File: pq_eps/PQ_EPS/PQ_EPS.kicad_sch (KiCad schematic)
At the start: 87 parts, among them IC1 DS2782E+, IC2 ISL9120IRTNZ, J1 CES-110-02-L-S, J2 CES-110-02-L-S, J3 CES-110-02-L-S, J4 CES-110-02-L-S, Q1 SIR424DP, U1 SPV1040TTR, U2 SPV1040TTR, U3 SPV1040TTR, U4 LTC4040EUFD#PBF

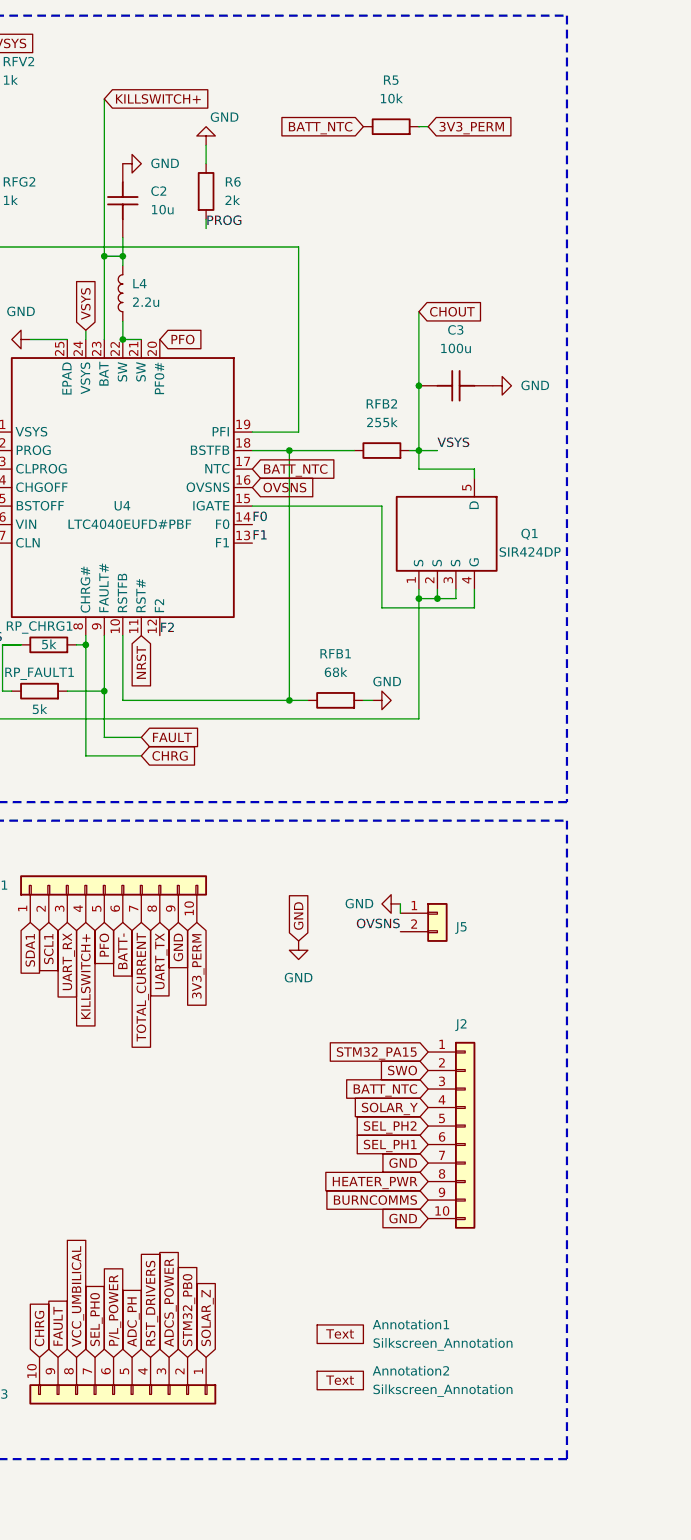
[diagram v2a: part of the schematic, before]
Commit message: small changes: change ID R5 to Rbias, add snail logo, and swap SOLARZ with GND
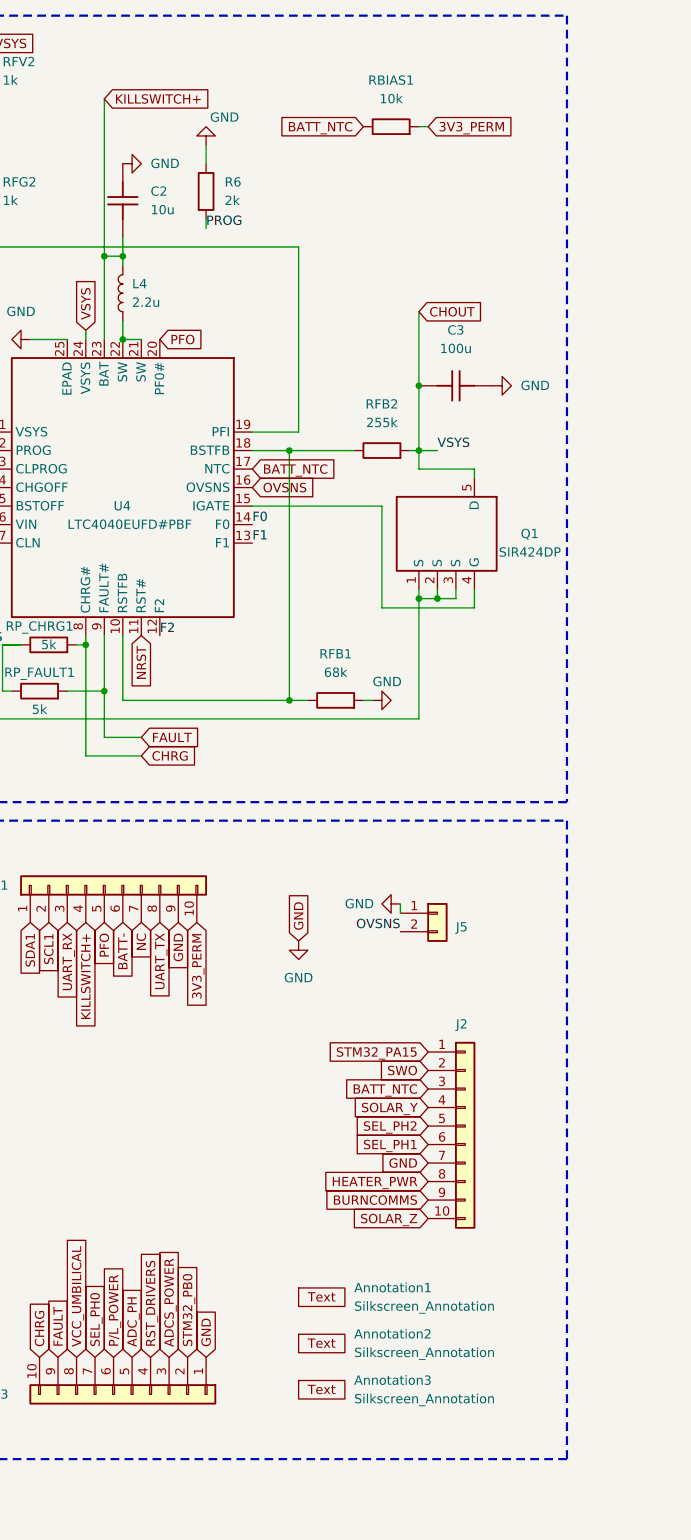
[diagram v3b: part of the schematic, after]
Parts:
- added Annotation3: Silkscreen_Annotation, symbols-nsl:Snail, symbol symbols-nsl:Silkscreen_Annotation
- renumbered R5 to RBIAS1
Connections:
- net GND: now also J3.1 (Pin_1); no longer J2.10 (Pin_10)
- net SOLAR_Z: now also J2.10 (Pin_10); no longer J3.1 (Pin_1)
- net TOTAL_CURRENT renamed NC
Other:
- moved on the sheet: Annotation1, Annotation2
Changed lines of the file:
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@@
     )
   )
-  (global_label "SOLAR_Z" (shape input) (at 297.18 210.82 90) (fields_autoplaced)
+  (global_label "GND" (shape input) (at 297.18 210.82 90) (fields_autoplaced)
     (effects (font (size 1.27 1.27)) (justify left))
-    (property "Intersheetrefs" "${INTERSHEET_REFS}" (at 297.1006 200.3031 90)
+    (property "Intersheetrefs" "${INTERSHEET_REFS}" (at 297.18 203.9643 90)
       (effects (font (size 1.27 1.27)) (justify left) hide)
     )
@@
     )
   )
-  (global_label "GND" (shape input) (at 327.66 191.77 180) (fields_autoplaced)
+  (global_label "SOLAR_Z" (shape input) (at 327.66 191.77 180) (fields_autoplaced)
     (effects (font (size 1.27 1.27)) (justify right))
-    (property "Intersheetrefs" "${INTERSHEET_REFS}" (at 321.3764 191.6906 0)
+    (property "Intersheetrefs" "${INTERSHEET_REFS}" (at 316.571 191.77 0)
       (effects (font (size 1.27 1.27)) (justify right) hide)
     )
@@
     )
   )
-  (global_label "TOTAL_CURRENT" (shape input) (at 288.29 151.13 270) (fields_autoplaced)
+  (global_label "NC" (shape input) (at 288.29 151.13 270) (fields_autoplaced)
     (effects (font (size 1.27 1.27)) (justify right))
-    (property "Intersheetrefs" "${INTERSHEET_REFS}" (at 288.2106 168.4807 90)
+    (property "Intersheetrefs" "${INTERSHEET_REFS}" (at 288.29 156.7157 90)
       (effects (font (size 1.27 1.27)) (justify right) hide)
     )
@@
     )
   )
-  (symbol (lib_id "symbols-nsl:Silkscreen_Annotation") (at 313.69 213.36 0) (unit 1)
+  (symbol (lib_id "symbols-nsl:Silkscreen_Annotation") (at 311.15 208.28 0) (unit 1)
     (in_bom yes) (on_board yes) (dnp no) (fields_autoplaced)
-    (property "Reference" "Annotation1" (at 320.04 206.375 0)
+    (property "Reference" "Annotation1" (at 317.5 201.295 0)
       (effects (font (size 1.27 1.27)) (justify left))
     )
-    (property "Value" "Silkscreen_Annotation" (at 320.04 208.915 0)
+    (property "Value" "Silkscreen_Annotation" (at 317.5 203.835 0)
       (effects (font (size 1.27 1.27)) (justify left))
     )
-    (property "Footprint" "symbols-nsl:Bridgemaker" (at 313.69 213.36 0)
+    (property "Footprint" "symbols-nsl:Bridgemaker" (at 311.15 208.28 0)
       (effects (font (size 1.27 1.27)) hide)
     )
-    (property "Datasheet" "" (at 313.69 213.36 0)
+    (property "Datasheet" "" (at 311.15 208.28 0)
       (effects (font (size 1.27 1.27)) hide)
     )
@@
   (symbol (lib_id "Device:R") (at 322.58 41.91 90) (unit 1)
     (in_bom yes) (on_board yes) (dnp no) (fields_autoplaced)
-    (property "Reference" "R5" (at 322.58 35.56 90)
+    (property "Reference" "RBIAS1" (at 322.58 35.56 90)
       (effects (font (size 1.27 1.27)))
     )
@@
       (project "PQ_EPS"
         (path "/369ed984-4bc0-4563-9a96-3c71b74c6c81"
-          (reference "R5") (unit 1)
+          (reference "RBIAS1") (unit 1)
         )
       )
@@
     )
   )
+  (symbol (lib_id "symbols-nsl:Silkscreen_Annotation") (at 311.15 220.98 0) (unit 1)
+    (in_bom yes) (on_board yes) (dnp no) (fields_autoplaced)
+    (property "Reference" "Annotation3" (at 317.5 213.995 0)
+      (effects (font (size 1.27 1.27)) (justify left))
+    )
+    (property "Value" "Silkscreen_Annotation" (at 317.5 216.535 0)
+      (effects (font (size 1.27 1.27)) (justify left))
+    )
+    (property "Footprint" "symbols-nsl:Snail" (at 311.15 220.98 0)
+      (effects (font (size 1.27 1.27)) hide)
+    )
+    (property "Datasheet" "" (at 311.15 220.98 0)
+      (effects (font (size 1.27 1.27)) hide)
+    )
+    (instances
+      (project "PQ_EPS"
+        (path "/369ed984-4bc0-4563-9a96-3c71b74c6c81"
+          (reference "Annotation3") (unit 1)
+        )
+      )
+    )
+  )
   (symbol (lib_id "Mechanical:MountingHole_Pad") (at 113.03 233.68 0) (unit 1)
     (in_bom yes) (on_board yes) (dnp no) (fields_autoplaced)
@@
     )
   )
-  (symbol (lib_id "symbols-nsl:Silkscreen_Annotation") (at 313.69 219.71 0) (unit 1)
+  (symbol (lib_id "symbols-nsl:Silkscreen_Annotation") (at 311.15 214.63 0) (unit 1)
     (in_bom yes) (on_board yes) (dnp no) (fields_autoplaced)
-    (property "Reference" "Annotation2" (at 320.04 212.725 0)
+    (property "Reference" "Annotation2" (at 317.5 207.645 0)
       (effects (font (size 1.27 1.27)) (justify left))
     )
-    (property "Value" "Silkscreen_Annotation" (at 320.04 215.265 0)
+    (property "Value" "Silkscreen_Annotation" (at 317.5 210.185 0)
       (effects (font (size 1.27 1.27)) (justify left))
     )
-    (property "Footprint" "symbols-nsl:NakNak" (at 313.69 219.71 0)
+    (property "Footprint" "symbols-nsl:NakNak" (at 311.15 214.63 0)
       (effects (font (size 1.27 1.27)) hide)
     )
-    (property "Datasheet" "" (at 313.69 219.71 0)
+    (property "Datasheet" "" (at 311.15 214.63 0)
       (effects (font (size 1.27 1.27)) hide)
     )

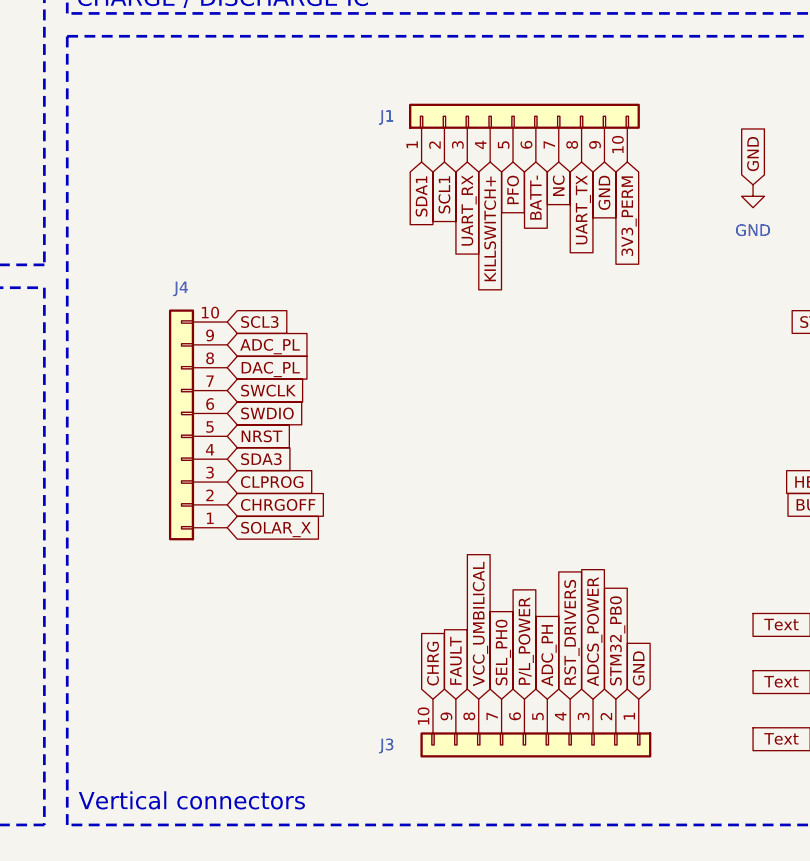
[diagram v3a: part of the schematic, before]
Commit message: change RST_DRIVERS to STM32_PA9, swap SCL3 with NC, and change NC to PH_PL
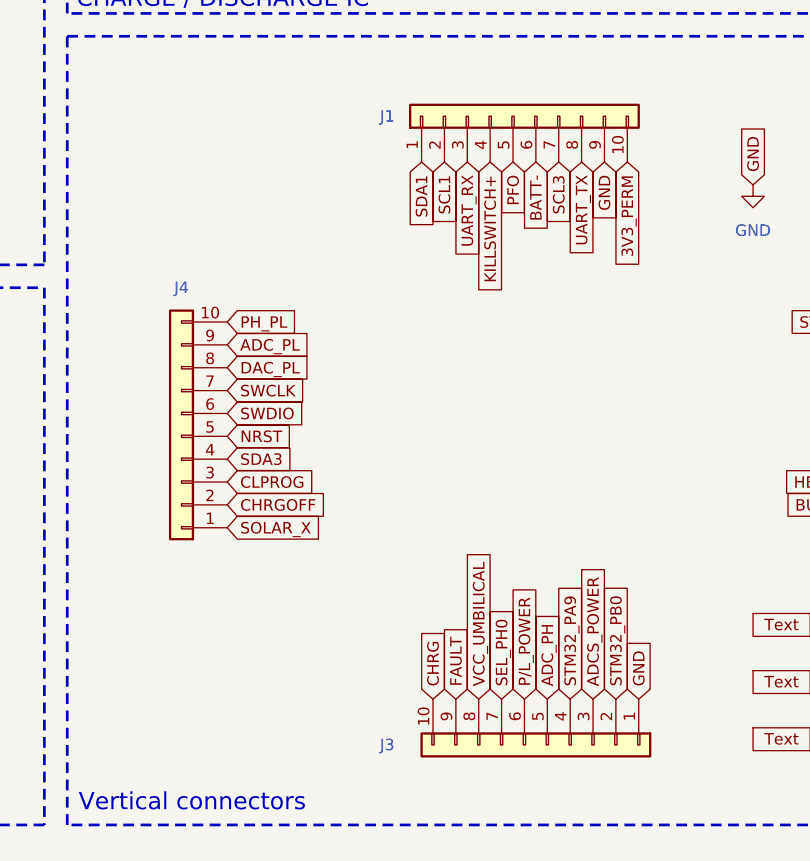
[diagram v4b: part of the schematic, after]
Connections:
- net NC is gone; now on net SCL3: J1.7 (Pin_7)
- net SCL3: no longer J4.10 (Pin_10)
- net RST_DRIVERS renamed STM32_PA9
- new net PH_PL: J4.10 (Pin_10)
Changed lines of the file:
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@@
     )
   )
-  (global_label "SCL3" (shape input) (at 251.46 168.91 0) (fields_autoplaced)
-    (effects (font (size 1.27 1.27)) (justify left))
-    (property "Intersheetrefs" "${INTERSHEET_REFS}" (at 258.5902 168.8306 0)
+  (global_label "PH_PL" (shape input) (at 251.46 168.91 0) (fields_autoplaced)
+    (effects (font (size 1.27 1.27)) (justify left))
+    (property "Intersheetrefs" "${INTERSHEET_REFS}" (at 260.3114 168.91 0)
       (effects (font (size 1.27 1.27)) (justify left) hide)
     )
@@
     )
   )
-  (global_label "NC" (shape input) (at 288.29 151.13 270) (fields_autoplaced)
-    (effects (font (size 1.27 1.27)) (justify right))
-    (property "Intersheetrefs" "${INTERSHEET_REFS}" (at 288.29 156.7157 90)
+  (global_label "SCL3" (shape input) (at 288.29 151.13 270) (fields_autoplaced)
+    (effects (font (size 1.27 1.27)) (justify right))
+    (property "Intersheetrefs" "${INTERSHEET_REFS}" (at 288.29 158.8323 90)
       (effects (font (size 1.27 1.27)) (justify right) hide)
     )
@@
     )
   )
-  (global_label "RST_DRIVERS" (shape input) (at 289.56 210.82 90) (fields_autoplaced)
-    (effects (font (size 1.27 1.27)) (justify left))
-    (property "Intersheetrefs" "${INTERSHEET_REFS}" (at 289.4806 196.1302 90)
-      (effects (font (size 1.27 1.27)) (justify left) hide)
-    )
+  (global_label "STM32_PA9" (shape input) (at 289.56 210.82 90) (fields_autoplaced)
+    (effects (font (size 1.27 1.27)) (justify left))
+    (property "Intersheetrefs" "${INTERSHEET_REFS}" (at 289.56 197.2516 90)
+      (effects (font (size 1.27 1.27)) (justify left) hide)
+    )

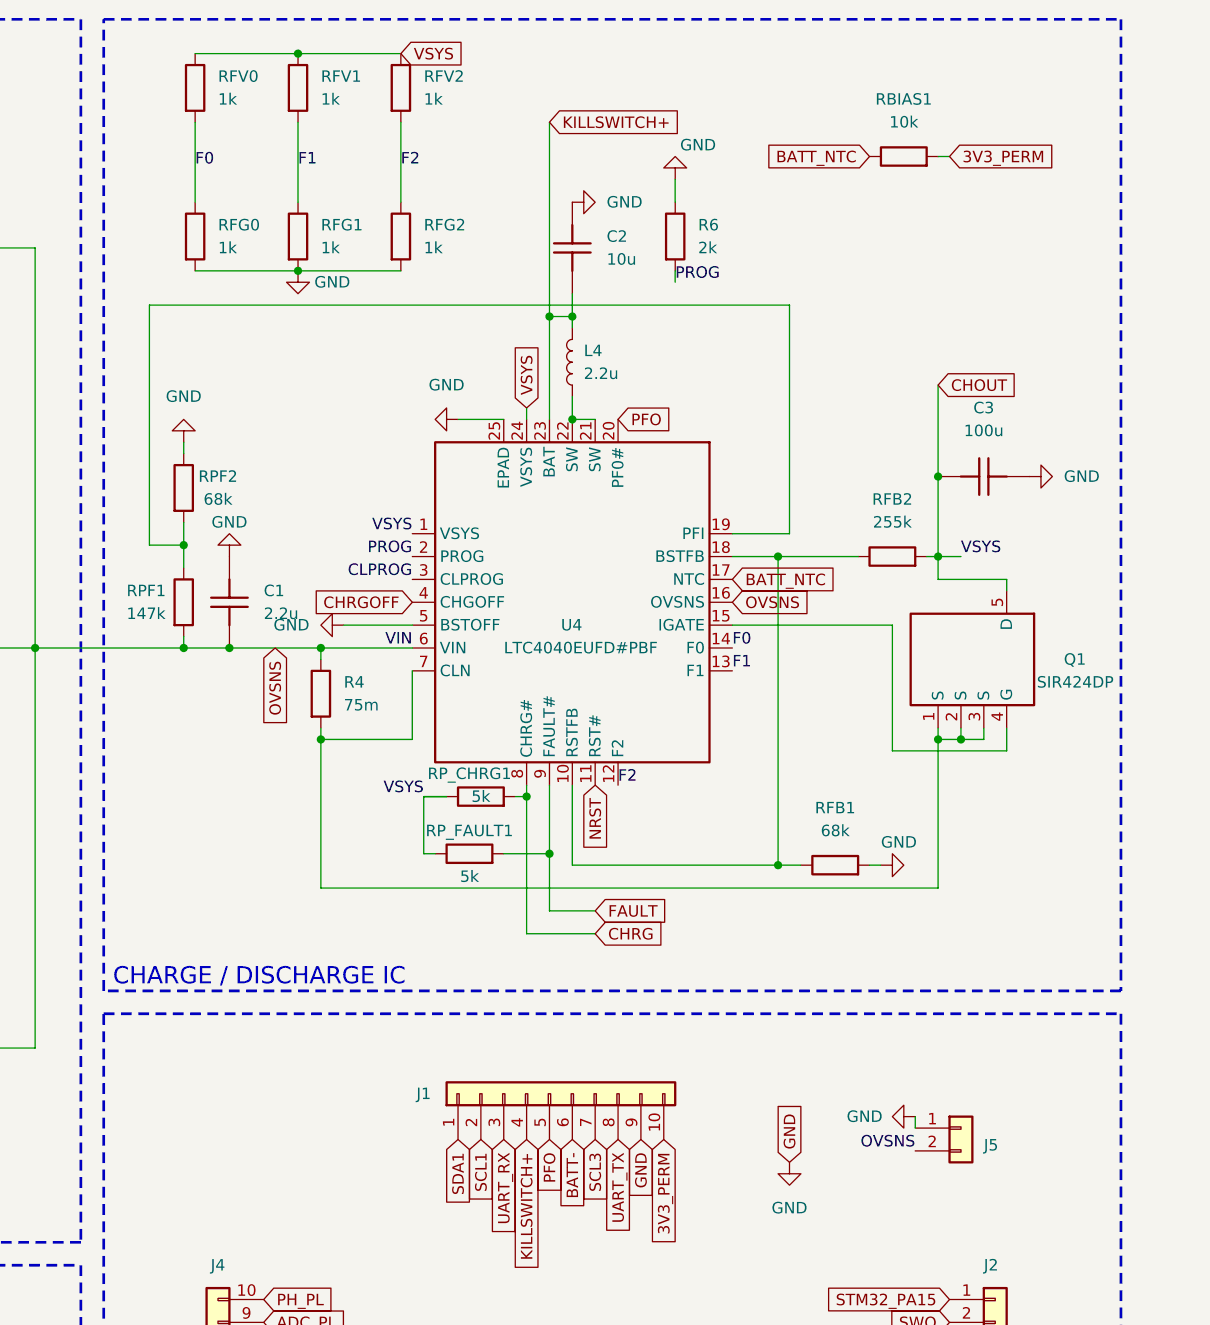
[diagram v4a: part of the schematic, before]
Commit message: Cambiar etiquetas de red a etiquetas globales (Major RID 66)
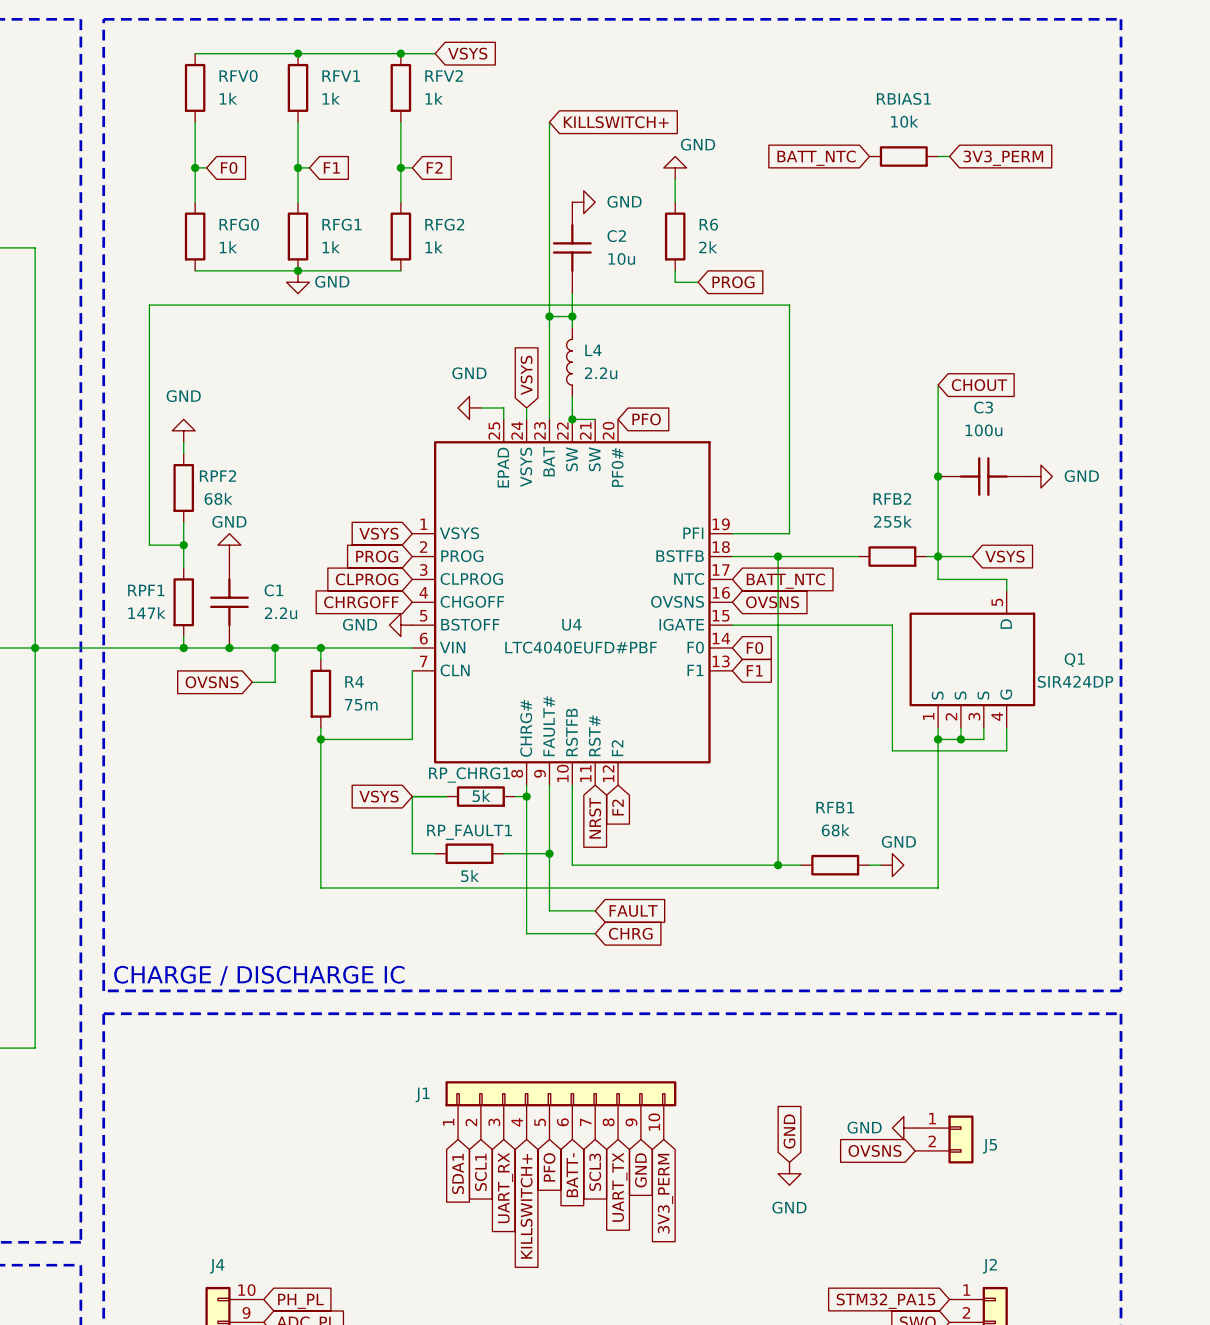
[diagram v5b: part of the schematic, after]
